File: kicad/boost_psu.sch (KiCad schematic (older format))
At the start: 18 parts, among them J1 +12V, J2 HT, Q1 MPSA55, Q2 IRF740, U1 MC34063AP

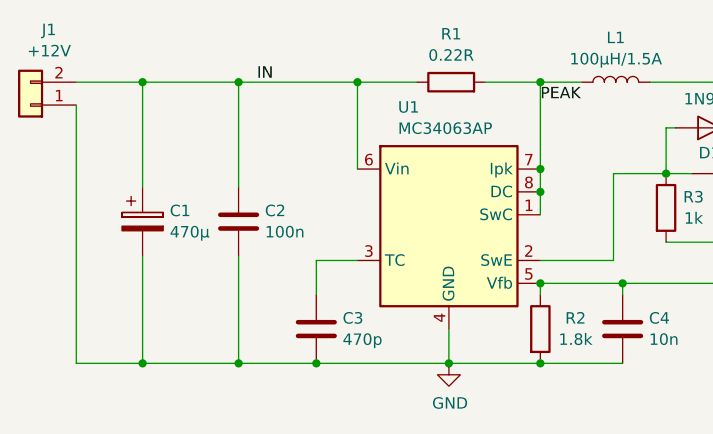
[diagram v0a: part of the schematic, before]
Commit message: Improve schematic & PCB routing
- put filtering capacitors on the switch collector rather than Vin
- add a 100n filtering capacitor on Vin
- switch to a 30x50mm board for a better layout
- add LEMON Amps as co-author

Signed-off-by: Arnaud Ferraris <arnaud.ferraris@gmail.com>
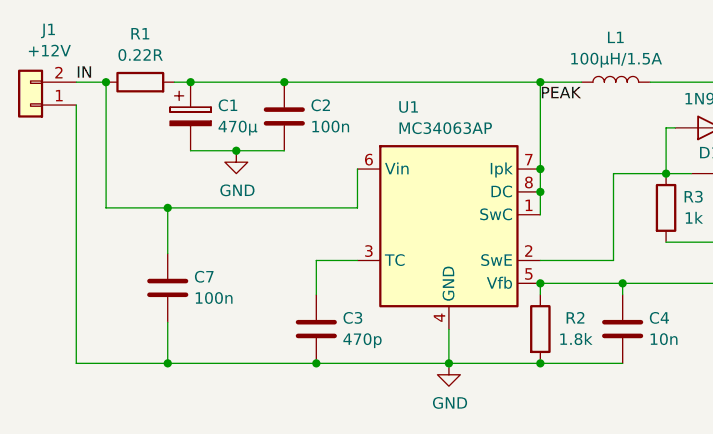
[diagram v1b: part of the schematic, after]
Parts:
- added C7: 100n, Capacitor_THT:C_Rect_L7.2mm_W3.0mm_P5.00mm_FKS2_FKP2_MKS2_MKP2, symbol Device:C
- C5: footprint Capacitor_THT:C_Disc_D10.5mm_W5.0mm_P7.50mm -> Capacitor_THT:C_Disc_D10.5mm_W5.0mm_P5.00mm
- L1: footprint Inductor_THT:L_Radial_D10.5mm_P5.00mm_Abacron_AISR-01 -> ProjectLib:L_Radial_D10.5mm_P5.00mm_MuRATA_1200RS
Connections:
- net GND: now also C7.2
- net IN: now also C7.1; no longer C1.1, C2.1
- net PEAK: now also C1.1, C2.1
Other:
- moved on the sheet: C1, C2, R1
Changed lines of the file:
@@
 Date "2019-03-07"
 Rev "0"
-Comp "Arnaud Ferraris (A-wai Amplification)"
+Comp "Arnaud Ferraris (A-wai Amplification) & LEMON Amps"
 Comment1 "Licensed under CERN OHL v.1.2"
 Comment2 ""
 Comment3 ""
-Comment4 ""
+Comment4 "Tube preamplifier power supply"
 $EndDescr
 $Comp
@@
 L Device:C C2
 U 1 1 5C811D18
-P 3920 4010
-F 0 "C2" H 4035 4057 50  0000 L CNN
-F 1 "100n" H 4035 3964 50  0000 L CNN
-F 2 "Capacitor_THT:C_Rect_L7.2mm_W3.0mm_P5.00mm_FKS2_FKP2_MKS2_MKP2" H 3958 3860 50  0001 C CNN
-F 3 "~" H 3920 4010 50  0001 C CNN
-	1    3920 4010
+P 4120 3550
+F 0 "C2" H 4235 3597 50  0000 L CNN
+F 1 "100n" H 4235 3504 50  0000 L CNN
+F 2 "Capacitor_THT:C_Rect_L7.2mm_W3.0mm_P5.00mm_FKS2_FKP2_MKS2_MKP2" H 4158 3400 50  0001 C CNN
+F 3 "~" H 4120 3550 50  0001 C CNN
+	1    4120 3550
 	1    0    0    -1
 $EndComp
@@
 L Device:CP C1
 U 1 1 5C811E08
-P 3500 4010
-F 0 "C1" H 3619 4057 50  0000 L CNN
-F 1 "470µ" H 3619 3964 50  0000 L CNN
-F 2 "Capacitor_THT:CP_Radial_D10.0mm_P5.00mm" H 3538 3860 50  0001 C CNN
-F 3 "~" H 3500 4010 50  0001 C CNN
-	1    3500 4010
+P 3710 3550
+F 0 "C1" H 3829 3597 50  0000 L CNN
+F 1 "470µ" H 3829 3504 50  0000 L CNN
+F 2 "Capacitor_THT:CP_Radial_D10.0mm_P5.00mm" H 3748 3400 50  0001 C CNN
+F 3 "~" H 3710 3550 50  0001 C CNN
+	1    3710 3550
 	1    0    0    -1
 $EndComp
@@
 F 0 "L1" V 5764 3400 50  0000 C CNN
 F 1 "100µH/1.5A" V 5671 3400 50  0000 C CNN
-F 2 "Inductor_THT:L_Radial_D10.5mm_P5.00mm_Abacron_AISR-01" H 5570 3400 50  0001 C CNN
+F 2 "ProjectLib:L_Radial_D10.5mm_P5.00mm_MuRATA_1200RS" H 5570 3400 50  0001 C CNN
 F 3 "~" H 5570 3400 50  0001 C CNN
 	1    5570 3400
@@
 L Device:R R1
 U 1 1 5C81278F
-P 4850 3400
-F 0 "R1" V 5060 3400 50  0000 C CNN
-F 1 "0.22R" V 4967 3400 50  0000 C CNN
-F 2 "Resistor_THT:R_Axial_DIN0207_L6.3mm_D2.5mm_P7.62mm_Horizontal" V 4780 3400 50  0001 C CNN
-F 3 "~" H 4850 3400 50  0001 C CNN
-	1    4850 3400
+P 3490 3400
+F 0 "R1" V 3700 3400 50  0000 C CNN
+F 1 "0.22R" V 3607 3400 50  0000 C CNN
+F 2 "Resistor_THT:R_Axial_DIN0207_L6.3mm_D2.5mm_P7.62mm_Horizontal" V 3420 3400 50  0001 C CNN
+F 3 "~" H 3490 3400 50  0001 C CNN
+	1    3490 3400
 	0    -1   -1   0
 $EndComp
-Wire Wire Line
-	5000 3400 5240 3400
 Wire Wire Line
 	5240 3400 5240 3780
 Connection ~ 5240 3780
-Wire Wire Line
-	4700 3400 4440 3400
-Wire Wire Line
-	4440 3400 4440 3780
 $Comp
 L Device:R R3
@@
 F 0 "C5" H 7295 3807 50  0000 L CNN
 F 1 "100n" H 7295 3714 50  0000 L CNN
-F 2 "Capacitor_THT:C_Disc_D10.5mm_W5.0mm_P7.50mm" H 7218 3610 50  0001 C CNN
+F 2 "Capacitor_THT:C_Disc_D10.5mm_W5.0mm_P5.00mm" H 7218 3610 50  0001 C CNN
 F 3 "~" H 7180 3760 50  0001 C CNN
 	1    7180 3760
@@
 	8540 3560 8540 3500
 Wire Wire Line
-	3210 3400 3500 3400
-Connection ~ 4440 3400
-Wire Wire Line
-	4260 4630 3920 4630
-Wire Wire Line
 	3210 4630 3210 3500
 Connection ~ 4260 4630
-Wire Wire Line
-	3920 3860 3920 3400
-Connection ~ 3920 3400
-Wire Wire Line
-	3920 3400 4440 3400
-Wire Wire Line
-	3500 3860 3500 3400
-Connection ~ 3500 3400
-Wire Wire Line
-	3500 3400 3920 3400
-Wire Wire Line
-	3500 4160 3500 4630
-Connection ~ 3500 4630
-Wire Wire Line
-	3500 4630 3210 4630
-Wire Wire Line
-	3920 4160 3920 4630
-Connection ~ 3920 4630
-Wire Wire Line
-	3920 4630 3500 4630
 Text Label 6120 3400 0    50   ~ 0
 HT1
@@
 Text Label 7730 3400 0    50   ~ 0
 HT2
-Text Label 4000 3400 0    50   ~ 0
+Text Label 3210 3400 0    50   ~ 0
 IN
+Wire Wire Line
+	3210 4630 3610 4630
+Wire Wire Line
+	3640 3400 3710 3400
+Connection ~ 3710 3400
+Wire Wire Line
+	3710 3400 4120 3400
+Connection ~ 4120 3400
+Wire Wire Line
+	4120 3400 5240 3400
+Wire Wire Line
+	3710 3700 3910 3700
+$Comp
+L power:GND #PWR04
+U 1 1 5C83F408
+P 3910 3700
+F 0 "#PWR04" H 3910 3450 50  0001 C CNN
+F 1 "GND" H 3915 3525 50  0000 C CNN
+F 2 "" H 3910 3700 50  0001 C CNN
+F 3 "" H 3910 3700 50  0001 C CNN
+	1    3910 3700
+	1    0    0    -1
+$EndComp
+Connection ~ 3910 3700
+Wire Wire Line
+	3910 3700 4120 3700
+Wire Wire Line
+	3210 3400 3340 3400
+Wire Wire Line
+	3340 3400 3340 3950
+Wire Wire Line
+	3340 3950 3610 3950
+Wire Wire Line
+	4440 3950 4440 3780
+Connection ~ 3340 3400
+$Comp
+L Device:C C7
+U 1 1 5C840E90
+P 3610 4300
+F 0 "C7" H 3725 4347 50  0000 L CNN
+F 1 "100n" H 3725 4254 50  0000 L CNN
+F 2 "Capacitor_THT:C_Rect_L7.2mm_W3.0mm_P5.00mm_FKS2_FKP2_MKS2_MKP2" H 3648 4150 50  0001 C CNN
+F 3 "~" H 3610 4300 50  0001 C CNN
+	1    3610 4300
+	1    0    0    -1
+$EndComp
+Wire Wire Line
+	3610 4450 3610 4630
+Connection ~ 3610 4630
+Wire Wire Line
+	3610 4630 4260 4630
+Wire Wire Line
+	3610 4150 3610 3950
+Connection ~ 3610 3950
+Wire Wire Line
+	3610 3950 4440 3950
 $EndSCHEMATC

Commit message: Change a few footprints and rework schematics
Signed-off-by: Arnaud Ferraris <arnaud.ferraris@gmail.com>
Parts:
- C3: footprint Capacitor_THT:C_Rect_L7.2mm_W3.0mm_P5.00mm_FKS2_FKP2_MKS2_MKP2 -> Capacitor_THT:C_Disc_D6.0mm_W4.4mm_P5.00mm
- C4: value 10n -> 100n
- C5: value 100n -> 10n/400V; footprint Capacitor_THT:C_Disc_D10.5mm_W5.0mm_P5.00mm -> Capacitor_THT:C_Disc_D6.0mm_W4.4mm_P5.00mm
- C6: footprint Capacitor_THT:CP_Radial_D13.0mm_P5.00mm -> Capacitor_THT:CP_Radial_D10.0mm_P5.00mm
- D1: value 1N914 -> 1N4148
- Q1: value MPSA55 -> MPS751; symbol Device:Q_PNP_CBE -> Device:Q_PNP_EBC
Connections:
- net GND: now also Q1.1 (E); no longer Q1.3 (E)
- net at D1.1 (K), Q2.1 (G): now also Q1.3 (C); no longer Q1.1 (C)
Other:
- note added: "Iout\n\n35mA\n25mA\n70mA\n50mA"
- note added: "L1\n\n100µH\n100µH\n220µH\n220µH"
- note added: "R4 and L1 values can be adjusted\nfor different input/ouput voltages.\nBelow are a few examples:"
- note added: "R4\n\n330k\n430k\n330k\n430k"
- note added: "Vin\n\n12V\n12V\n24V\n24V"
- note added: "Vout\n\n230V\n300V\n230V\n300V"
- moved on the sheet: C1, C2, C3, C4, C5, C6, C7, D1, D2, J1, J2, L1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

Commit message: Fix transistor polarity
Signed-off-by: Arnaud Ferraris <arnaud.ferraris@gmail.com>
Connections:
- net GND: now also Q1.3 (C); no longer Q1.1 (E)
- net at D1.1 (K), Q2.1 (G): now also Q1.1 (E); no longer Q1.3 (C)
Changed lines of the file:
@@
 F 3 "~" H 5390 3030 50  0001 C CNN
 	1    5390 3030
-	1    0    0    -1
+	1    0    0    1
 $EndComp
 $Comp

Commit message: Add BOM
Signed-off-by: Arnaud Ferraris <arnaud.ferraris@gmail.com>
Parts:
- C1: MFR (none) -> Nichicon; MPN (none) -> UVR1V471MPD; SPN (none) -> 862-3370; SPR (none) -> RS; SPURL (none) -> -
- C2, C4, C7: MFR (none) -> WIMA; MPN (none) -> MKS2D031001A00KI00; SPN (none) -> 108-2700; SPR (none) -> RS; SPURL (none) -> -
- C3: MFR (none) -> KEMET; MPN (none) -> C322C471J2G5TA; SPN (none) -> 538-1534; SPR (none) -> RS; SPURL (none) -> -
- C5: MFR (none) -> KEMET; MPN (none) -> C322C103KBR5TA; SPN (none) -> 906-0654; SPR (none) -> RS; SPURL (none) -> -
- C6: MFR (none) -> Nichicon; MPN (none) -> UBT2V4R7MPD8; SPN (none) -> 762-189; SPR (none) -> RS; SPURL (none) -> -
- D1: MFR (none) -> ON Semiconductor; MPN (none) -> 1N4148TR; SPN (none) -> 671-5477; SPR (none) -> RS; SPURL (none) -> -
- D2: MFR (none) -> Vishay; MPN (none) -> BYV26E-TAP; SPN (none) -> 708-7776; SPR (none) -> RS; SPURL (none) -> -
- J1, J2: MFR (none) -> Wurth Elektronik; MPN (none) -> 691102710002; SPN (none) -> 826-7226; SPR (none) -> RS; SPURL (none) -> -
- L1: MFR (none) -> Murata Power Solutions; MPN (none) -> 12RS104C; SPN (none) -> 715-7374; SPR (none) -> RS; SPURL (none) -> -
- Q1: MFR (none) -> ON Semiconductor; MPN (none) -> MPS751G; SPN (none) -> 774-3583; SPR (none) -> RS; SPURL (none) -> -
- Q2: MFR (none) -> Vishay; MPN (none) -> IRF740LCPBF; SPN (none) -> 536-5992; SPR (none) -> RS; SPURL (none) -> -
- R1: MFR (none) -> TE Connectivity; MPN (none) -> LR1F220R; SPN (none) -> 148-348; SPR (none) -> RS; SPURL (none) -> -
- R2: MFR (none) -> TE Connectivity; MPN (none) -> LR1F1K8; SPN (none) -> 148-562; SPR (none) -> RS; SPURL (none) -> -
- R3: MFR (none) -> TE Connectivity; MPN (none) -> LR1F1K0; SPN (none) -> 125-1159; SPR (none) -> RS; SPURL (none) -> -
- R4: MFR (none) -> TE Connectivity; MPN (none) -> YR1B432KCC; SPN (none) -> 754-5753; SPR (none) -> RS; SPURL (none) -> -
- U1: MFR (none) -> ON Semiconductor; MPN (none) -> MC34063AP1G; SPN (none) -> 516-5095; SPR (none) -> RS; SPURL (none) -> -

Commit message: Fix supplier refs in BOM
Signed-off-by: Arnaud Ferraris <arnaud.ferraris@gmail.com>
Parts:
- C6: SPN 762-189 -> 762-1890
- R4: SPN 754-5753 -> 754-5759

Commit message: Fix R1 Manufacturer & Supplier Part Nr.
Signed-off-by: Arnaud Ferraris <arnaud.ferraris@gmail.com>
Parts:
- R1: MPN LR1F220R -> LR1LJR22; SPN 148-348 -> 135-500
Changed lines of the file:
@@
 F 3 "~" H 2780 2630 50  0001 C CNN
 F 4 "TE Connectivity" H 0   0   50  0001 C CNN "MFR"
-F 5 "LR1F220R" H 0   0   50  0001 C CNN "MPN"
+F 5 "LR1LJR22" H 0   0   50  0001 C CNN "MPN"
 F 6 "RS" H 0   0   50  0001 C CNN "SPR"
-F 7 "148-348" H 0   0   50  0001 C CNN "SPN"
+F 7 "135-500" H 0   0   50  0001 C CNN "SPN"
 F 8 "-" H 0   0   50  0001 C CNN "SPURL"
 	1    2780 2630
